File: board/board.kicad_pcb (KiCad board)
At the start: 2 copper layers, 21 x 13 mm, 8 parts, among them J1 002_SPI, J2 012_CAN, U1 MCP2515-xSO, Y1 20MhZ

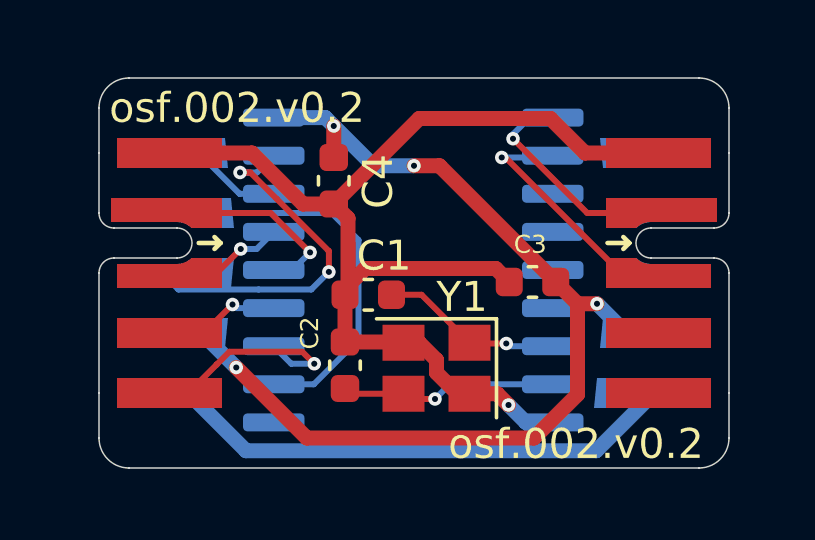
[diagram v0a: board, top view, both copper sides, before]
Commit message: updated to kicad 8.0 and 20pin tssop
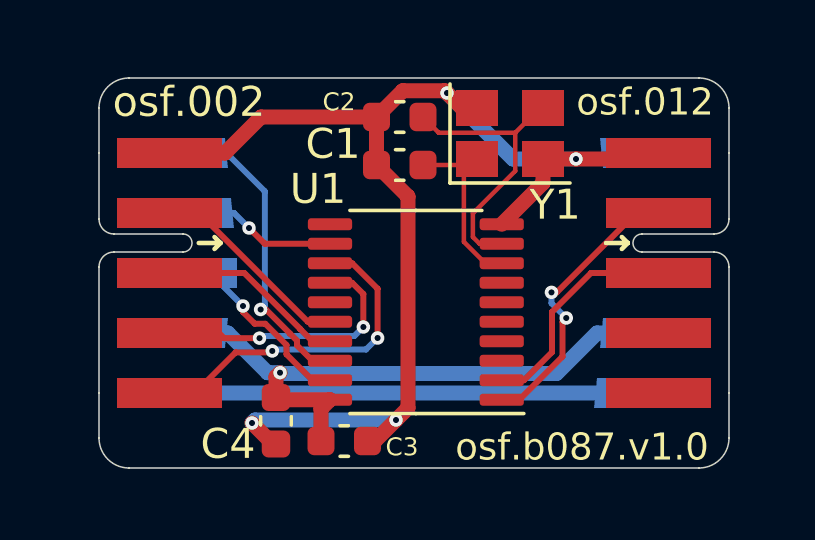
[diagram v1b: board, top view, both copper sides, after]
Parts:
- U1: value MCP2515-xSO -> MCP2515-xST; footprint Package_SO:SOIC-18W_7.5x11.6mm_P1.27mm -> Package_SO:TSSOP-20_4.4x6.5mm_P0.65mm; moved to F.Cu
- moved C2 8.47 mm to (87.0, 75.3), turned to 180 degrees
- moved C4 8.23 mm to (82.9, 85.4)
- moved C3 8.21 mm to (85.2, 86.1), turned to 0 degrees
- moved Y1 8.20 mm to (90.7, 75.8), turned to 0 degrees
- moved C1 4.45 mm to (87.0, 76.9)
- moved U1 1.40 mm to (87.6, 81.8)
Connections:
- C1 pad 1: Net-(C1-Pad1) -> Net-(U1-OSC2)
- C2 pad 1: Net-(C2-Pad1) -> Net-(U1-OSC1)
- C3 pad 1: +3V3 -> +3.3V
- C4 pad 1: +3V3 -> +3.3V
- J1 pad 9: +3V3 -> +3.3V
- J2 pad 5: unconnected-(J2-Pad5) -> (no net)
- J2 pad 6: unconnected-(J2-Pad6) -> (no net)
- J2 pad 7: unconnected-(J2-Pad7) -> (no net)
- J2 pad 8: unconnected-(J2-Pad8) -> (no net)
- J2 pad 9: +3V3 -> +3.3V
- U1 pad 10: unconnected-(U1-Pad10) -> GND
- U1 pad 11: /controller/INT0 -> unconnected-(U1-~{RX1BF}-Pad11)
- U1 pad 12: /controller/INT -> /controller/INT0
- U1 pad 13: /controller/CLK -> /controller/INT
- U1 pad 14: /controller/MOSI -> /controller/CLK
- U1 pad 15: /controller/MISO -> unconnected-(U1-NC-Pad15)
- U1 pad 16: /controller/CS -> /controller/MOSI
- U1 pad 17: /controller/RESET -> /controller/MISO
- U1 pad 18: +3V3 -> /controller/CS
- U1 pad 7: Net-(C1-Pad1) -> unconnected-(U1-~{TX2RTS}-Pad7)
- U1 pad 8: Net-(C2-Pad1) -> Net-(U1-OSC2)
- U1 pad 9: GND -> Net-(U1-OSC1)
- Y1 pad 1: Net-(C1-Pad1) -> Net-(U1-OSC2)
- Y1 pad 3: Net-(C2-Pad1) -> Net-(U1-OSC1)
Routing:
- net +3V3: track 35.4 -> 0.00 mm, vias 4 -> 0
- net +3.3V: track 0.00 -> 21.5 mm, vias 0 -> 1
- net Net-(U1-OSC1): track 0.00 -> 9.67 mm
- net /controller/INT0: track 13.7 -> 6.02 mm, vias 0 -> 1
- net Net-(C2-Pad1): track 7.27 -> 0.00 mm, vias 1 -> 0
- net /controller/CS: track 3.99 -> 10.8 mm, vias 0 -> 1
- net Net-(U1-OSC2): track 0.00 -> 6.38 mm
- net /controller/CLK: track 3.92 -> 10.2 mm, vias 1 -> 2
- net Net-(C1-Pad1): track 6.09 -> 0.00 mm, vias 1 -> 0
- net /controller/RESET: track 12.1 -> 6.88 mm, vias 2 -> 1
- net /controller/INT: track 7.15 -> 11.3 mm, vias 1 -> 2
- net /controller/MISO: track 2.79 -> 6.29 mm, vias 1 -> 0
- net /controller/CAN_TX: track 6.33 -> 9.68 mm, vias 1 -> 2
- net GND: track 37.9 -> 41.1 mm, vias 1 -> 4
- net /controller/MOSI: track 5.43 -> 6.85 mm, vias 1 -> 0
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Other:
- board text added: "osf.002"
- board text added: "osf.012"
- board text added: "osf.b087.v1.0"
- board text removed: "osf.002.v0.2"
- board text removed: "osf.b087.v0.1"

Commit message: added lcsc part numbers
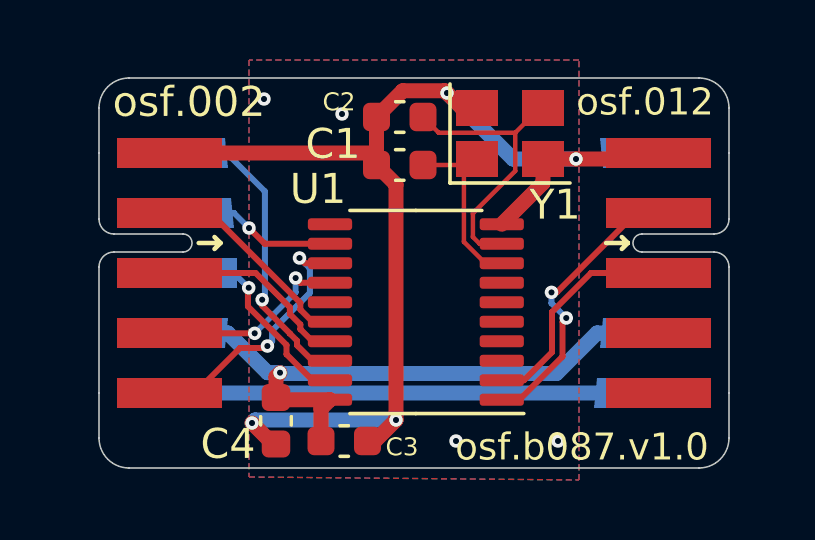
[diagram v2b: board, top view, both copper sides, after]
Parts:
- C1, C2: value 22pF -> 9pF
- Y1: value 20MhZ -> 16MhZ
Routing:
- net /controller/INT: track 11.3 -> 8.67 mm
- net /controller/CLK: track 10.2 -> 7.61 mm
- net GND: track 41.1 -> 41.5 mm, vias 4 -> 8
- added copper zone on B.Cu, net GND
- added copper zone on F.Cu, net GND
